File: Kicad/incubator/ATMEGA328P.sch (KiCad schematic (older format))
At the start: 5 parts, among them U2 ATmega328P-AU

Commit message: refactor: Kicad design updated
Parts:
- JP1: footprint Jumper:SolderJumper-2_P1.3mm_Bridged_RoundedPad1.0x1.5mm -> Jumper:SolderJumper-2_P1.3mm_Open_RoundedPad1.0x1.5mm
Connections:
- net VCC: now also U2.18 (AVCC)
- no-connect marks 9 -> 8
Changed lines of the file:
@@
 NoConn ~ 5575 2625
 NoConn ~ 5575 2425
-NoConn ~ 6275 2125
 NoConn ~ 6775 2425
 NoConn ~ 6775 2525
@@
 $EndComp
 Wire Wire Line
-	6175 2050 6325 2050
+	6175 2050 6275 2050
 $Comp
 L Jumper:SolderJumper_2_Open JP1
@@
 F 0 "JP1" V 5196 4037 50  0000 R CNN
 F 1 "SolderJumper_2_Open" V 5105 4037 50  0000 R CNN
-F 2 "Jumper:SolderJumper-2_P1.3mm_Bridged_RoundedPad1.0x1.5mm" H 5150 4125 50  0001 C CNN
+F 2 "Jumper:SolderJumper-2_P1.3mm_Open_RoundedPad1.0x1.5mm" H 5150 4125 50  0001 C CNN
 F 3 "~" H 5150 4125 50  0001 C CNN
 	1    5150 4125
 	0    -1   -1   0
 $EndComp
+Wire Wire Line
+	6275 2125 6275 2050
+Connection ~ 6275 2050
+Wire Wire Line
+	6275 2050 6325 2050
 $EndSCHEMATC

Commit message: fix: fan size and push button position
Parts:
- C5, C6: symbol Device:C -> incubator-rescue:C-Device
- JP1: symbol Jumper:SolderJumper_2_Open -> incubator-rescue:SolderJumper_2_Open-Jumper
- R5: symbol Device:R -> incubator-rescue:R-Device
- U2: symbol MCU_Microchip_ATmega:ATmega328P-AU -> incubator-rescue:ATmega328P-AU-MCU_Microchip_ATmega
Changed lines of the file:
@@
 $EndDescr
 $Comp
-L MCU_Microchip_ATmega:ATmega328P-AU U2
+L incubator-rescue:ATmega328P-AU-MCU_Microchip_ATmega U2
 U 1 1 610AABC9
 P 6175 3625
@@
 $EndComp
 $Comp
-L Device:C C6
+L incubator-rescue:C-Device C6
 U 1 1 610AABD5
 P 4925 2275
+AR Path="/610AABD5" Ref="C6"  Part="1"
+AR Path="/61116939/610AABD5" Ref="C6"  Part="1"
 F 0 "C6" H 5040 2321 50  0000 L CNN
 F 1 "100n" H 5040 2230 50  0000 L CNN
@@
 $EndComp
 $Comp
-L Device:C C5
+L incubator-rescue:C-Device C5
 U 1 1 610AABDB
 P 4600 2275
+AR Path="/610AABDB" Ref="C5"  Part="1"
+AR Path="/61116939/610AABDB" Ref="C5"  Part="1"
 F 0 "C5" H 4715 2321 50  0000 L CNN
 F 1 "10u" H 4715 2230 50  0000 L CNN
@@
 Connection ~ 4925 2050
 $Comp
-L power:GND #PWR0115
+L incubator-rescue:GND-power #PWR0115
 U 1 1 610AABE5
 P 4600 2525
@@
 Connection ~ 4600 2475
 $Comp
-L power:VCC #PWR0116
+L incubator-rescue:VCC-power #PWR0116
 U 1 1 610AABF0
 P 5150 3400
@@
 ~RESET
 $Comp
-L Device:R R5
+L incubator-rescue:R-Device R5
 U 1 1 610AAC20
 P 5150 3675
+AR Path="/610AAC20" Ref="R5"  Part="1"
+AR Path="/61116939/610AAC20" Ref="R5"  Part="1"
 F 0 "R5" H 5220 3721 50  0000 L CNN
 F 1 "100k" H 5220 3630 50  0000 L CNN
@@
 D7
 $Comp
-L power:GND #PWR0117
+L incubator-rescue:GND-power #PWR0117
 U 1 1 610AAC01
 P 5150 4350
@@
 GND
 $Comp
-L power:GND #PWR0118
+L incubator-rescue:GND-power #PWR0118
 U 1 1 610AAC08
 P 6175 5250
@@
 	6175 1975 6175 2050
 $Comp
-L power:VCC #PWR0119
+L incubator-rescue:VCC-power #PWR0119
 U 1 1 610AABCF
 P 6175 1975
@@
 	6175 2050 6275 2050
 $Comp
-L Jumper:SolderJumper_2_Open JP1
+L incubator-rescue:SolderJumper_2_Open-Jumper JP1
 U 1 1 610E209B
 P 5150 4125

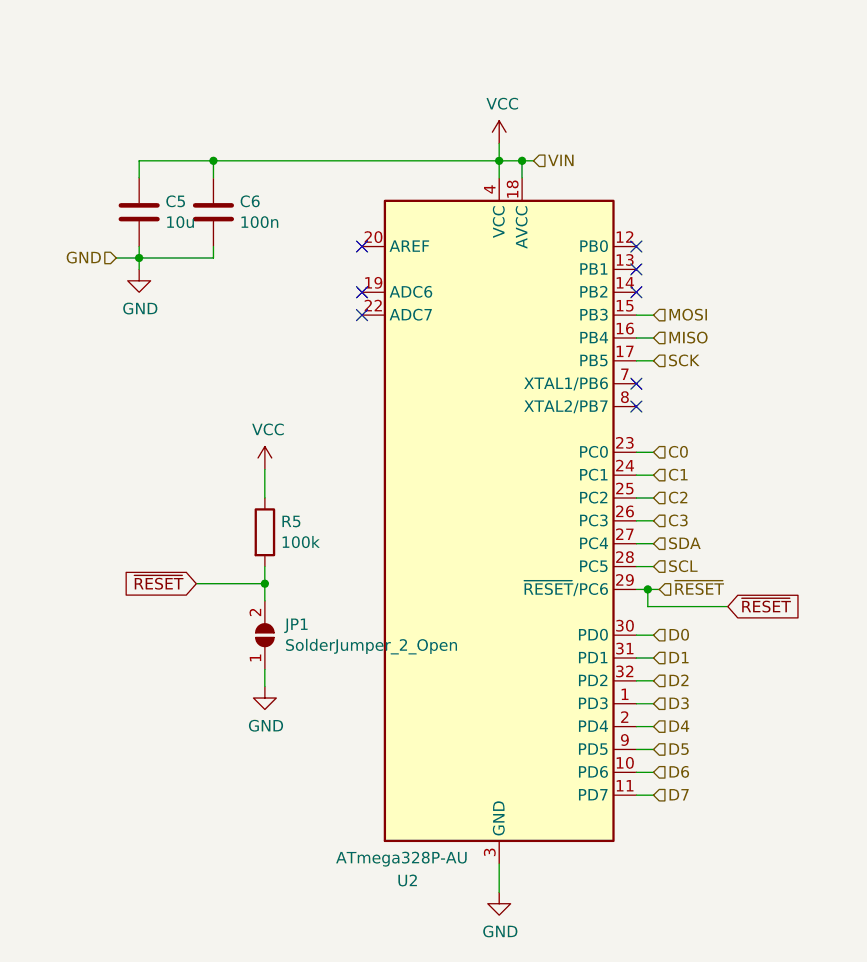
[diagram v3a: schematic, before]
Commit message: fix: iss #1: add ERROR and BLINKING LED, iss #2: solved
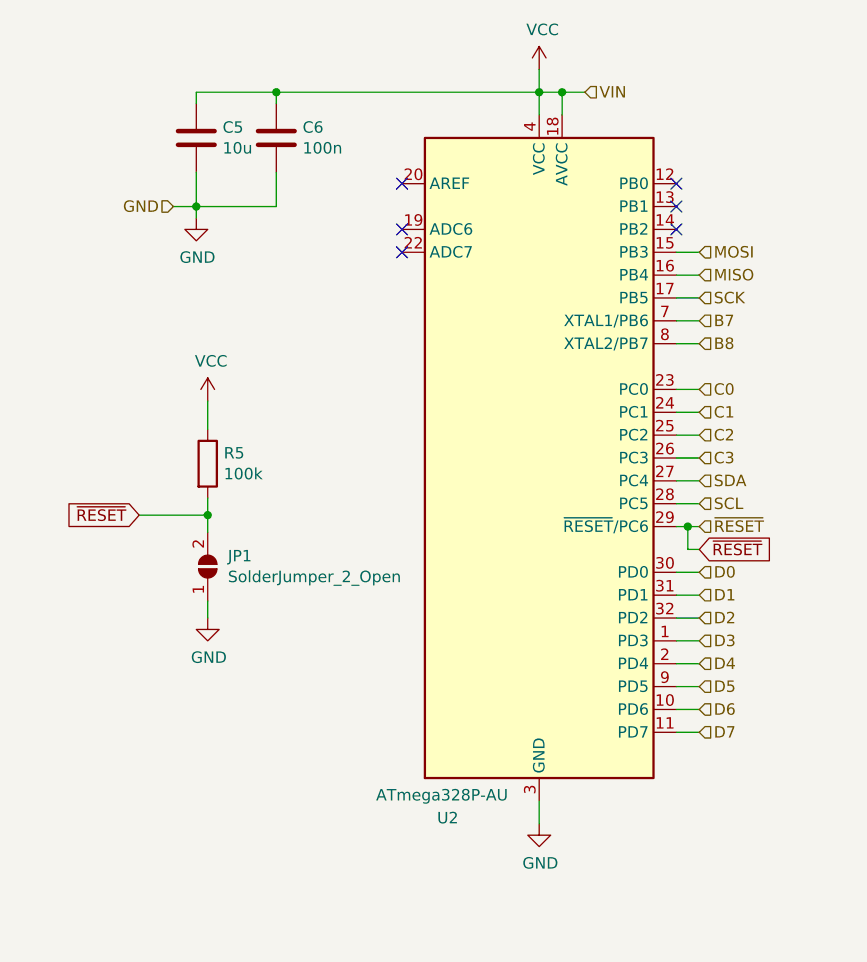
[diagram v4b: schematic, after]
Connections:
- net B7: now reaches U2.7 (XTAL1/PB6)
- net B8: now reaches U2.8 (XTAL2/PB7)
- no-connect marks 8 -> 6
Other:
- moved on the sheet: C5, C6, JP1, R5, U2
